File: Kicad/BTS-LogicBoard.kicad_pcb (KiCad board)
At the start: 2 copper layers, 41.9 x 55.9 mm, 58 parts, among them J1 Conn_02x03_Odd_Even, J2 Conn_01x03, J3 Conn_01x02, J4 Conn_02x03_Odd_Even, J5 Conn_01x06, Q1 BC817, U1 NCS2252SN2T1G, U2 NE555DR/TS555, U3 74HC1GU04, U4 TLP291, U5 74HC1GU04, U6 NCS2252SN2T1G, U8 LM1117-5.0

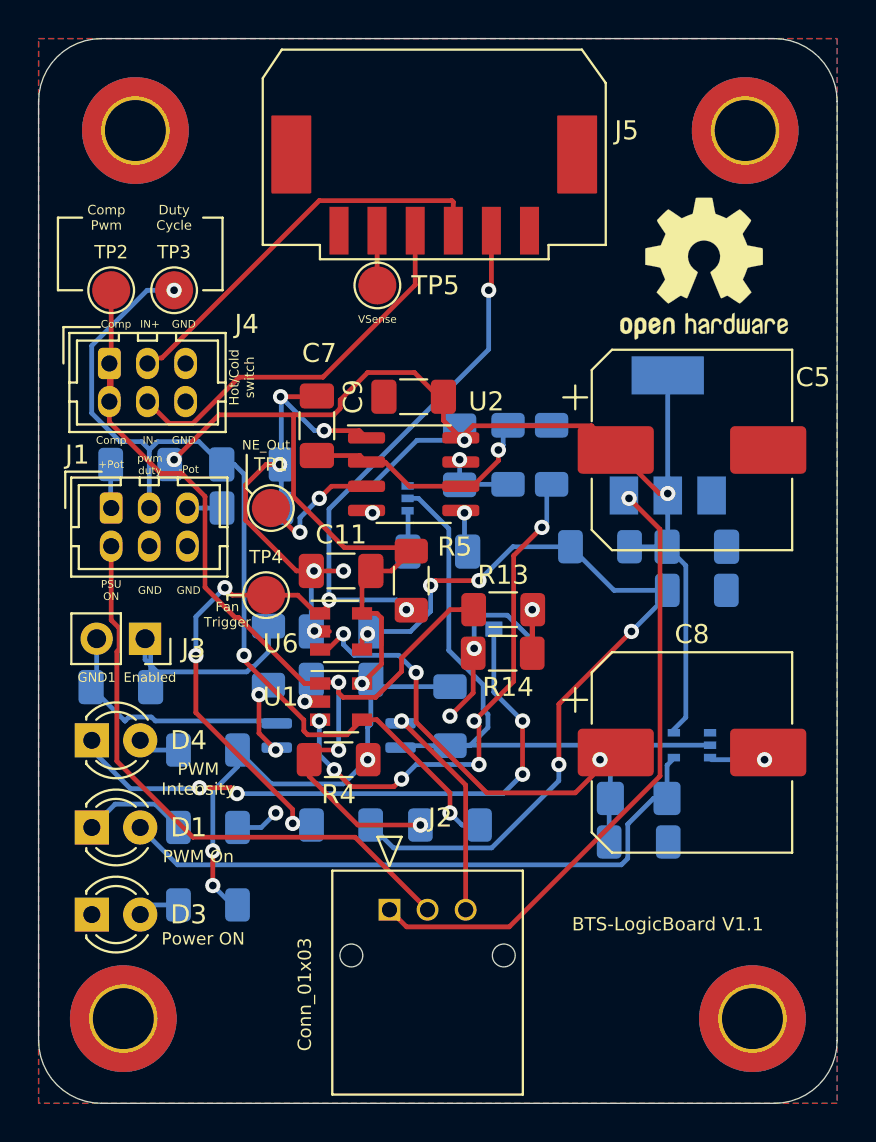
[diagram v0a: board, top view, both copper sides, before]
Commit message: Forgot to add another hysteresis resistor : done
Signed-off-by: bebenlebricolo <benoittarrade@hotmail.fr>
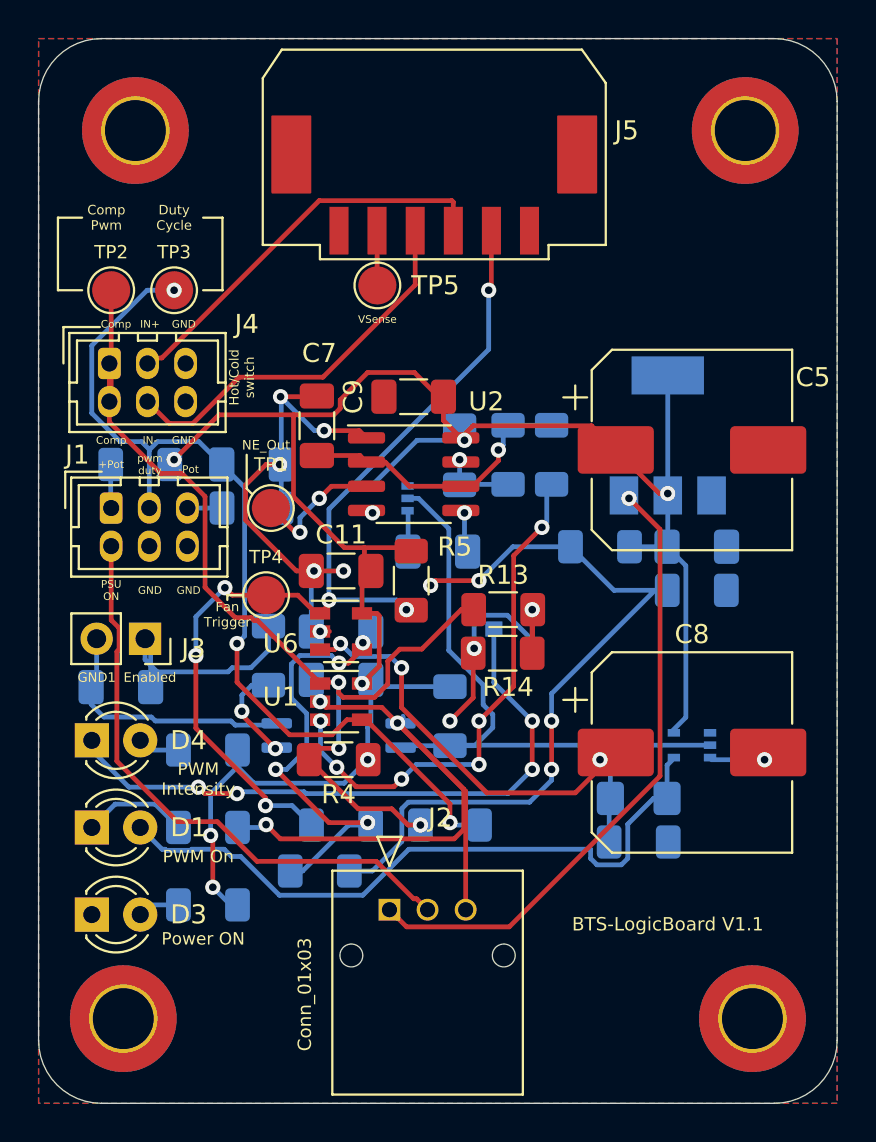
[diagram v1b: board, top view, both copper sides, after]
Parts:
- removed REF**: KiCad-Logo2_5mm_SilkScreen, Symbol:KiCad-Logo2_5mm_SilkScreen
- removed REF**: OSHW-Logo2_9.8x8mm_SilkScreen, Symbol:OSHW-Logo2_9.8x8mm_SilkScreen
- added R19: 4.7k, Resistor_SMD:R_1206_3216Metric_Pad1.30x1.75mm_HandSolder, B.Cu at (126.5, 109.7)
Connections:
- C12 pad 1: /2.5V -> Net-(C12-Pad1)
- R18 pad 2: /2.5V -> Net-(C12-Pad1)
- U6 pad 4: /2.5V -> Net-(C12-Pad1)
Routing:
- net Net-(C12-Pad1): track 0.00 -> 23.8 mm, vias 0 -> 4
- net GND: track 59.1 -> 80.5 mm
- net /2.5V: track 44.5 -> 40.9 mm, vias 5 -> 4
- net Net-(D1-Pad2): track 33.1 -> 35.4 mm
- net VCC: track 108.6 -> 107.1 mm
- net Net-(R20-Pad1): track 4.00 -> 5.17 mm
- net Net-(C8-Pad1): track 27.6 -> 26.5 mm
- net Net-(D4-Pad1): track 32.3 -> 32.9 mm
- net GND1: track 13.5 -> 14.0 mm
